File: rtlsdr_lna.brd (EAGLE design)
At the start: 34.3 x 12.7 mm, 18 parts, among them U1 MIC5205-3

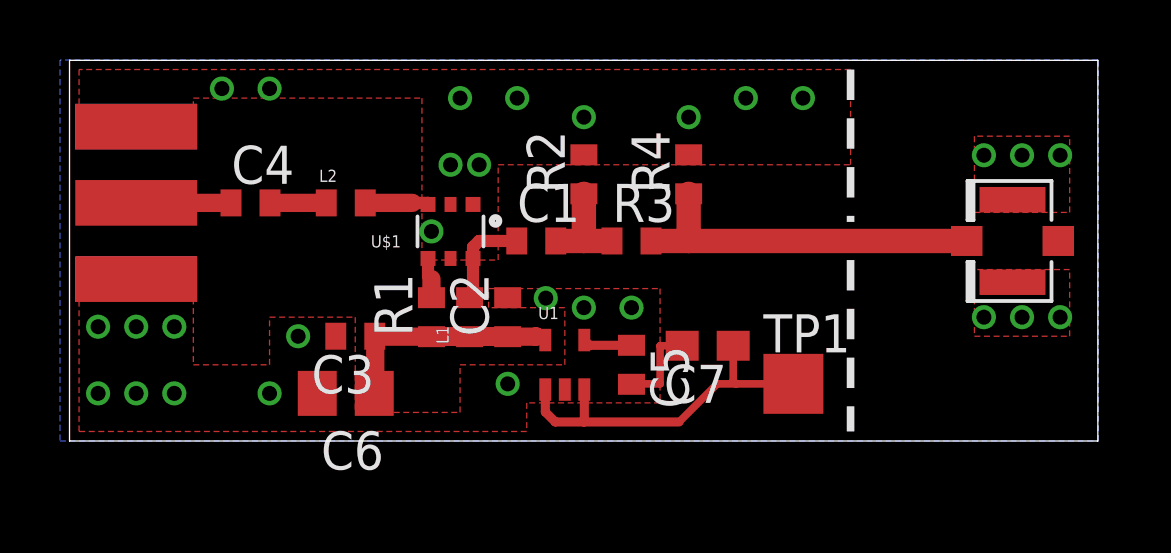
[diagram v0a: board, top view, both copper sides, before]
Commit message: increased inductor package size, added missing ldo and rbias component values
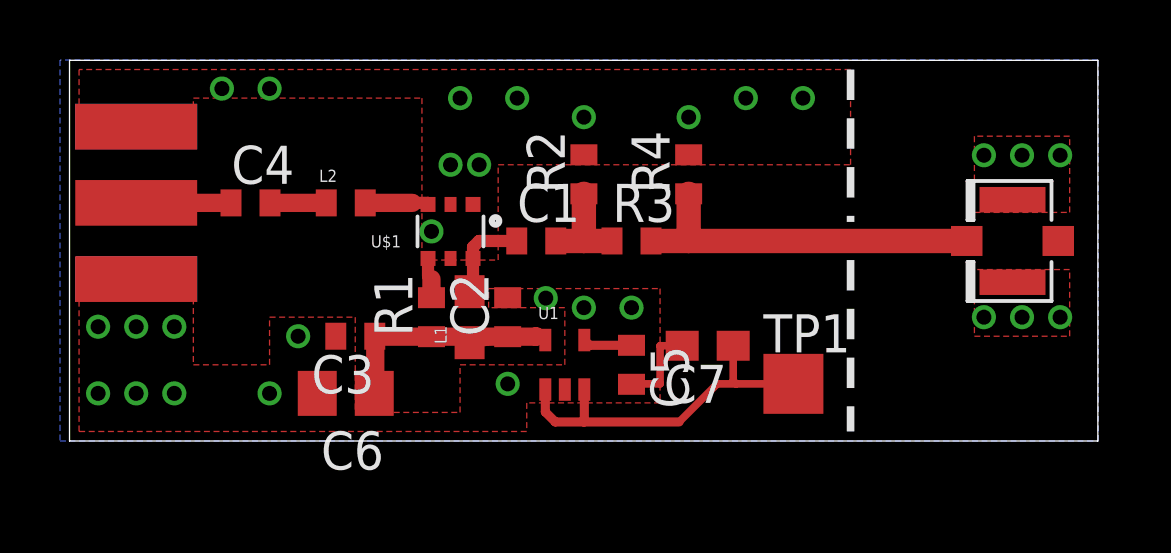
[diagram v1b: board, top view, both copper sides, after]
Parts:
- C7: value (none) -> .1uF
- L1: value (none) -> 47nH; device SparkFun-Passives:C0402 -> SparkFun-Passives:0603
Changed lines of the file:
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@@
 <element name="C3" library="rcl" package="C0402" value="10nF" x="9.8425" y="3.4925" rot="R180"/>
 <element name="C4" library="rcl" package="C0402" value="100pF" x="6.35" y="7.9375"/>
-<element name="L1" library="SparkFun-Passives" package="C0402" value="" x="13.6525" y="4.1275" rot="R90"/>
+<element name="L1" library="SparkFun-Passives" package="0603" value="47nH" x="13.6525" y="4.1275" rot="R90"/>
 <element name="R2" library="rcl" package="R0402" value="DNP" x="17.4625" y="8.89" rot="R90"/>
 <element name="R3" library="rcl" package="R0402" value="JMP" x="19.05" y="6.6675"/>
@@
 </element>
 <element name="C6" library="rcl" package="C0805" value="4.7uF, TANT" x="9.525" y="1.5875" rot="R180"/>
-<element name="C7" library="rcl" package="C0603" value="" x="21.59" y="3.175" rot="R180"/>
+<element name="C7" library="rcl" package="C0603" value=".1uF" x="21.59" y="3.175" rot="R180"/>
 </elements>
 <signals>
@@
 <wire x1="13.7675" y1="6.465" x2="13.97" y2="6.6675" width="0.4064" layer="1"/>
 <wire x1="13.7675" y1="6.085" x2="13.7675" y2="4.8925" width="0.4064" layer="1"/>
-<wire x1="13.7675" y1="4.8925" x2="13.6525" y2="4.7775" width="0.4064" layer="1"/>
+<wire x1="13.7675" y1="4.8925" x2="13.6525" y2="4.9775" width="0.4064" layer="1"/>
 </signal>
 <signal name="N$5">
@@
 <contactref element="R1" pad="1"/>
 <contactref element="C6" pad="1"/>
-<wire x1="12.3825" y1="3.4775" x2="13.6525" y2="3.4775" width="0.6096" layer="1"/>
-<wire x1="13.6525" y1="3.4775" x2="14.9225" y2="3.4775" width="0.6096" layer="1"/>
-<wire x1="14.9225" y1="3.4775" x2="10.5075" y2="3.4775" width="0.6096" layer="1"/>
+<wire x1="14.9225" y1="3.4775" x2="12.3825" y2="3.4775" width="0.6096" layer="1"/>
+<wire x1="12.3825" y1="3.4775" x2="10.5075" y2="3.4775" width="0.6096" layer="1"/>
 <wire x1="10.5075" y1="3.4775" x2="10.4925" y2="3.4925" width="0.6096" layer="1" curve="-90"/>
 <wire x1="10.5075" y1="3.4775" x2="10.5075" y2="1.62" width="0.6096" layer="1"/>
@@
 <wire x1="15.875" y1="3.4925" x2="15.86" y2="3.4775" width="0.6096" layer="1"/>
 <wire x1="15.86" y1="3.4775" x2="14.9225" y2="3.4775" width="0.6096" layer="1"/>
+<wire x1="12.3825" y1="3.4775" x2="13.6525" y2="3.4775" width="0.4064" layer="1"/>
+<wire x1="13.6525" y1="3.4775" x2="13.6525" y2="3.2775" width="0.4064" layer="1"/>
+<wire x1="13.6525" y1="3.2775" x2="14.9225" y2="3.4925" width="0.4064" layer="1"/>
 </signal>
 <signal name="N$7">

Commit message: changed values in matching network for improved S11 at lower frequencies (increased DC bias inductor value, increased DC blocking capacitor values to 330pF)
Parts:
- C1, C4: value 100pF -> 330pF
- L1: value 47nH -> 100nH
- L2: value 6.8nH -> 4.7nH
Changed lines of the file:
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@@
 <element name="U1" library="SparkFun-PowerIC" package="SC70" value="MIC5205-3" x="16.8275" y="2.54"/>
 <element name="R1" library="rcl" package="R0402" value="4.3k" x="12.3825" y="4.1275" rot="R90"/>
-<element name="C1" library="rcl" package="C0402" value="100pF" x="15.875" y="6.6675"/>
+<element name="C1" library="rcl" package="C0402" value="330pF" x="15.875" y="6.6675"/>
 <element name="C2" library="rcl" package="C0402" value="68pF" x="14.9225" y="4.1275" rot="R90"/>
 <element name="C3" library="rcl" package="C0402" value="10nF" x="9.8425" y="3.4925" rot="R180"/>
-<element name="C4" library="rcl" package="C0402" value="100pF" x="6.35" y="7.9375"/>
-<element name="L1" library="SparkFun-Passives" package="0603" value="47nH" x="13.6525" y="4.1275" rot="R90"/>
+<element name="C4" library="rcl" package="C0402" value="330pF" x="6.35" y="7.9375"/>
+<element name="L1" library="SparkFun-Passives" package="0603" value="100nH" x="13.6525" y="4.1275" rot="R90"/>
 <element name="R2" library="rcl" package="R0402" value="DNP" x="17.4625" y="8.89" rot="R90"/>
 <element name="R3" library="rcl" package="R0402" value="JMP" x="19.05" y="6.6675"/>
 <element name="R4" library="rcl" package="R0402" value="DNP" x="20.955" y="8.89" rot="R90"/>
 <element name="C5" library="rcl" package="C0402" value="470pF" x="19.05" y="2.54" rot="R270"/>
-<element name="L2" library="SparkFun-Passives" package="C0402" value="6.8nH" x="9.525" y="7.9375"/>
+<element name="L2" library="SparkFun-Passives" package="C0402" value="4.7nH" x="9.525" y="7.9375"/>
 <element name="J$1" library="SparkFun-Connectors" package="SMA-EDGE" value="SMA_EDGE" x="2.54" y="5.3975" rot="R90"/>
 <element name="U$2" library="SparkFun-Connectors" package="U.FL" value="U.FL" x="31.75" y="6.6675" rot="R180"/>

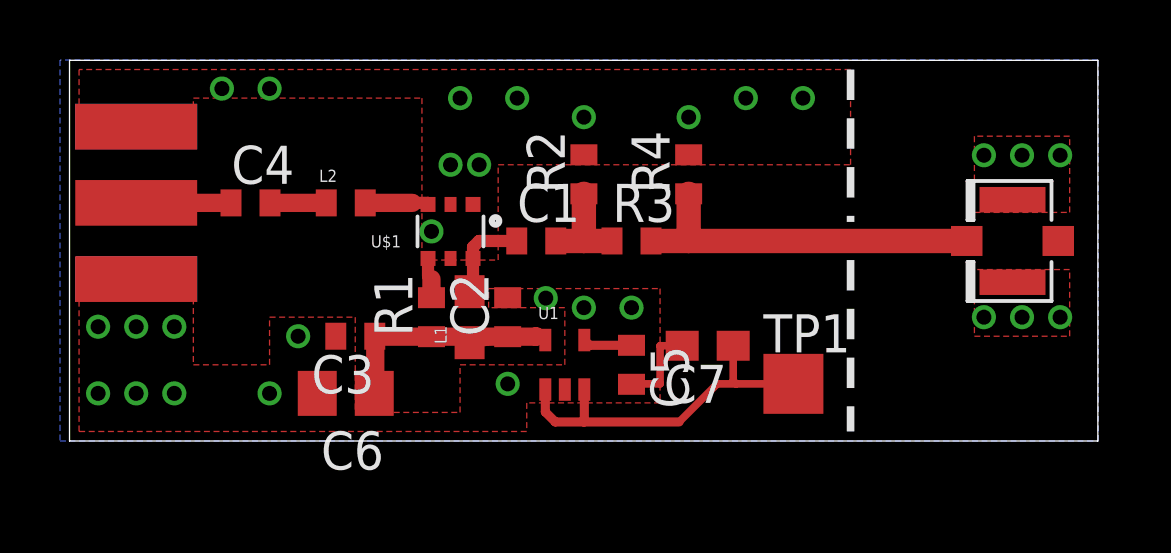
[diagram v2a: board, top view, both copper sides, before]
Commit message: reduced board size, increased clearances, changed voltage regulator footprint, added silkscreen and annotations
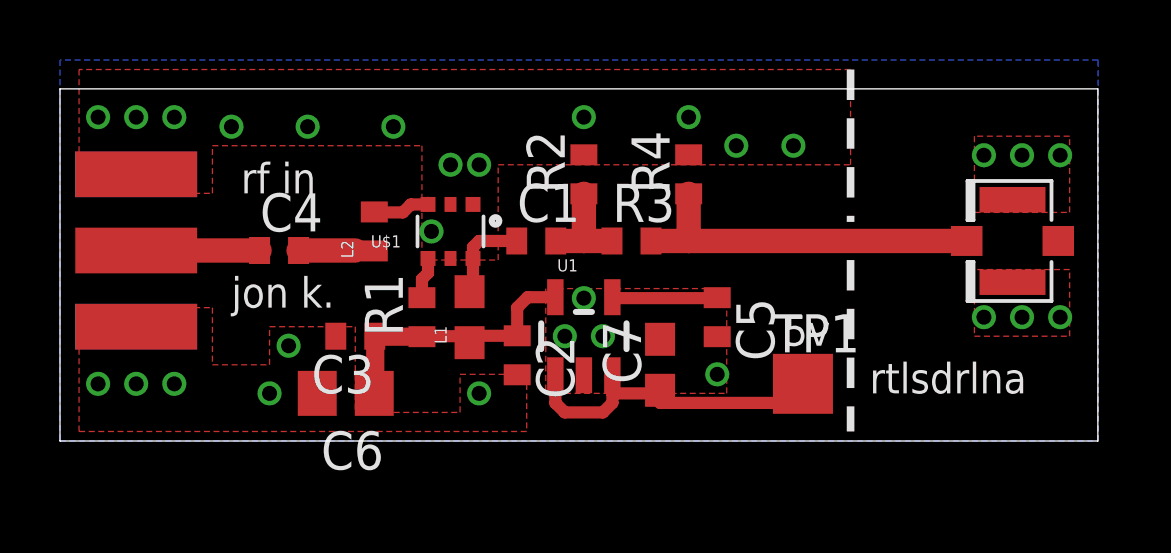
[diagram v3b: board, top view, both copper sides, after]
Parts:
- U1: device SparkFun-PowerIC:SC70 -> SparkFun-PowerIC:SOT23-5
- moved C5 3.27 mm to (21.9, 4.13)
- moved C4 1.85 mm to (7.30, 6.35)
- moved C7 1.71 mm to (20.0, 2.54), turned to 90 degrees
- moved J$1 1.59 mm to (2.54, 3.81)
- moved L2 1.35 mm to (10.5, 6.99), turned to 90 degrees
- moved C2 1.31 mm to (15.2, 2.86), turned to 270 degrees
- moved U1 1.14 mm to (17.5, 3.49)
- moved R1 0.32 mm to (12.1, 4.13)
- moved TP1 0.32 mm to (24.8, 1.91)
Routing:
- net GND: track 2.97 -> 0.00 mm
- net N$7: track 1.64 -> 3.52 mm
- net N$6: track 10.4 -> 9.35 mm
- net N$10: track 3.16 -> 4.11 mm
- net N$11: track 1.88 -> 2.53 mm
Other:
- board size 34.3 x 12.7 mm -> 34.6 x 11.7 mm
- board text added: "5v"
- board text added: "copper tape may be helpful"
- board text added: "cut here"
- board text added: "jon k."
- board text added: "rf in"
- board text added: "rtlsdrlna"
- board text added: "solder edge of board to f connector footprint"
- board text added: "soldermask removed on board edges"
- board text added: "units in mm"

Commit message: this time with the new layout and schematic..
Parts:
- C1, C4: value 330pF -> 180pF
- R1: value 4.3k -> 1k
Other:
- board text added: "solder edge of board to rf connector footprint"
- board text removed: "solder edge of board to f connector footprint"
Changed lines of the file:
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@@
 <text x="5.3975" y="24.4475" size="1.778" layer="47" font="vector">units in mm</text>
 <text x="-6.6675" y="-7.9375" size="1.27" layer="47" font="vector">soldermask removed on board edges</text>
-<text x="-6.6675" y="-10.795" size="1.27" layer="47" font="vector">solder edge of board to f connector footprint</text>
+<text x="-6.6675" y="-10.795" size="1.27" layer="47" font="vector">solder edge of board to rf connector footprint</text>
 <text x="-6.6675" y="-13.6525" size="1.27" layer="47" font="vector">copper tape may be helpful</text>
 </plain>
@@
 <element name="U$1" library="mr_radar" package="SOT363" value="MGA-68563" x="13.0175" y="6.985" rot="R180"/>
 <element name="U1" library="SparkFun-PowerIC" package="SOT23-5" value="MIC5205-3" x="17.4625" y="3.4925"/>
-<element name="R1" library="rcl" package="R0402" value="4.3k" x="12.065" y="4.1275" rot="R90"/>
-<element name="C1" library="rcl" package="C0402" value="330pF" x="15.875" y="6.6675"/>
+<element name="R1" library="rcl" package="R0402" value="1k" x="12.065" y="4.1275" rot="R90"/>
+<element name="C1" library="rcl" package="C0402" value="180pF" x="15.875" y="6.6675"/>
 <element name="C2" library="rcl" package="C0402" value="68pF" x="15.24" y="2.8575" rot="R270"/>
 <element name="C3" library="rcl" package="C0402" value="10nF" x="9.8425" y="3.4925" rot="R180"/>
-<element name="C4" library="rcl" package="C0402" value="330pF" x="7.3025" y="6.35"/>
+<element name="C4" library="rcl" package="C0402" value="180pF" x="7.3025" y="6.35"/>
 <element name="L1" library="SparkFun-Passives" package="0603" value="100nH" x="13.6525" y="4.1275" rot="R90"/>
 <element name="R2" library="rcl" package="R0402" value="DNP" x="17.4625" y="8.89" rot="R90"/>
